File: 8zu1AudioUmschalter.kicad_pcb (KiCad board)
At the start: 2 copper layers, 59 x 65 mm, 63 parts, among them IC1 ATMEGA8A-A, IC2 MAX9890, IC3 TMP75, J1 USB, J2 LUM 1503-07, J3 LUM 1503-07, J4 LUM 1503-07, J5 LUM 1503-07, J6 LUM 1503-07, J7 LUM 1503-07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

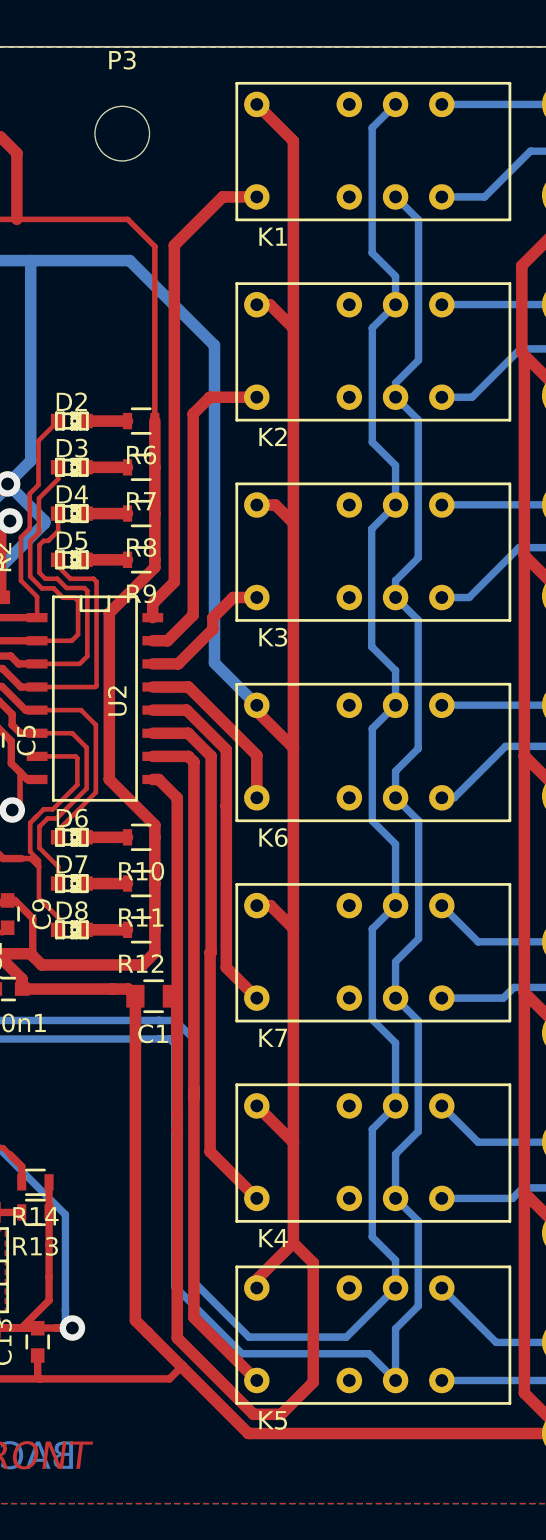
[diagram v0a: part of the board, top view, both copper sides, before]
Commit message: Leitungen zu den Relais auf die Back Layer gelegt
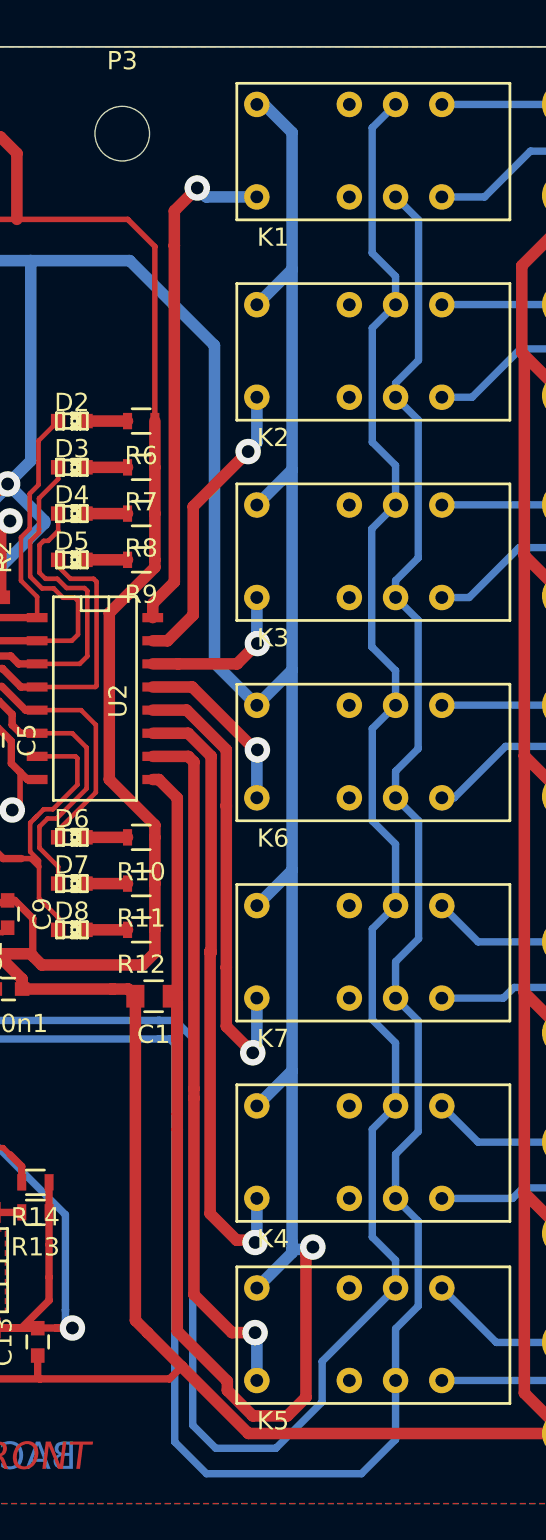
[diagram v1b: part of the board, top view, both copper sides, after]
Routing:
- net /CH_L_REL_IN: track 123.3 -> 134.5 mm
- net /CH_R_REL_IN: track 116.0 -> 127.0 mm
- net Net-(K7-Pad9): track 19.4 -> 25.4 mm, vias 0 -> 1
- net Net-(K4-Pad9): track 29.1 -> 34.7 mm, vias 0 -> 1
- net VCC: track 365.6 -> 367.2 mm, vias 6 -> 7
- net Net-(K1-Pad9): track 26.6 -> 28.1 mm, vias 0 -> 1
- net Net-(K2-Pad9): track 17.7 -> 16.2 mm, vias 0 -> 1
- net Net-(K3-Pad9): track 7.59 -> 8.75 mm, vias 0 -> 1
- net Net-(K5-Pad9): track 38.3 -> 39.0 mm, vias 0 -> 1
- net Net-(K6-Pad9): track 9.60 -> 9.82 mm, vias 0 -> 1

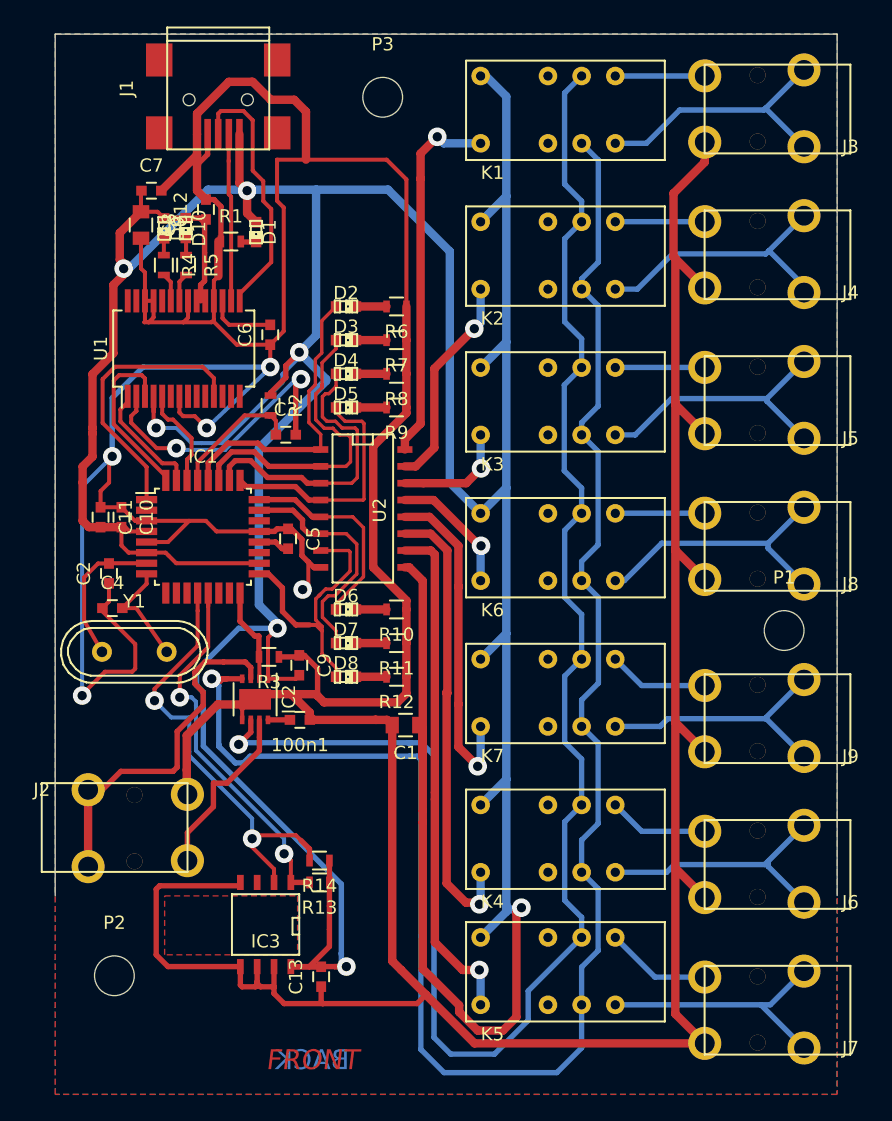
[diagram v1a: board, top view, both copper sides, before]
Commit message: Layoutfehler, TX und RX waren nicht gekreuzt.
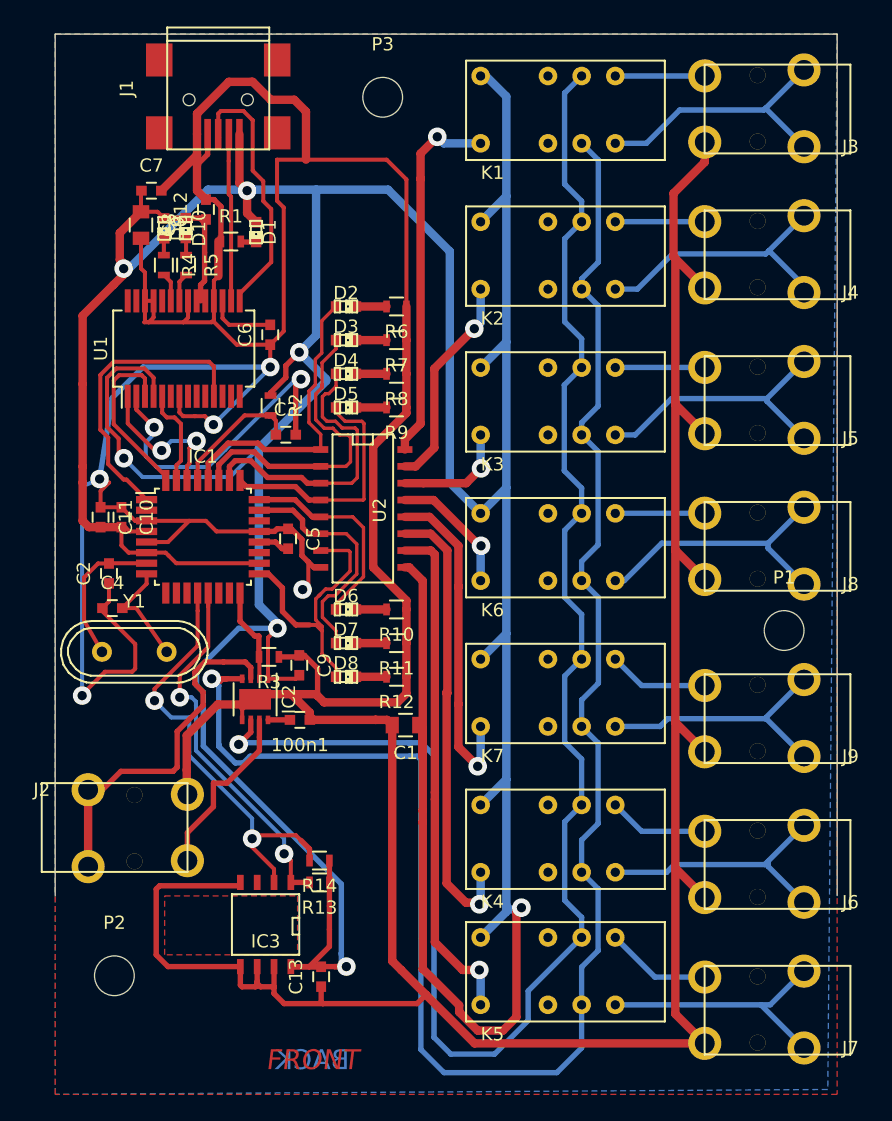
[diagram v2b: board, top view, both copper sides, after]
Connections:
- U1 pad 1: /TX -> /RX
- U1 pad 5: /RX -> /TX
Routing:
- net VCC: track 367.2 -> 372.6 mm
- net /RX: track 7.63 -> 12.2 mm, vias 0 -> 2
- net /DTR: track 22.6 -> 24.7 mm
- net /TX: track 8.88 -> 7.42 mm
- net /CTS: track 21.0 -> 22.4 mm
- net GND: track 425.5 -> 424.6 mm

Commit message: Umpolen der Relais, da diese eine bestimmte Polarität benötigen
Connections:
- K1 pad 8: VCC -> Net-(K1-Pad8)
- K1 pad 9: Net-(K1-Pad9) -> VCC
- K2 pad 8: VCC -> Net-(K2-Pad8)
- K2 pad 9: Net-(K2-Pad9) -> VCC
- K3 pad 8: VCC -> Net-(K3-Pad8)
- K3 pad 9: Net-(K3-Pad9) -> VCC
- K4 pad 8: VCC -> Net-(K4-Pad8)
- K4 pad 9: Net-(K4-Pad9) -> VCC
- K5 pad 8: VCC -> Net-(K5-Pad8)
- K5 pad 9: Net-(K5-Pad9) -> VCC
- K6 pad 8: VCC -> Net-(K6-Pad8)
- K6 pad 9: Net-(K6-Pad9) -> VCC
- K7 pad 8: VCC -> Net-(K7-Pad8)
- K7 pad 9: Net-(K7-Pad9) -> VCC
- U2 pad 10: Net-(K5-Pad9) -> Net-(K5-Pad8)
- U2 pad 11: Net-(K4-Pad9) -> Net-(K4-Pad8)
- U2 pad 12: Net-(K7-Pad9) -> Net-(K7-Pad8)
- U2 pad 13: Net-(K6-Pad9) -> Net-(K6-Pad8)
- U2 pad 14: Net-(K3-Pad9) -> Net-(K3-Pad8)
- U2 pad 15: Net-(K2-Pad9) -> Net-(K2-Pad8)
- U2 pad 16: Net-(K1-Pad9) -> Net-(K1-Pad8)
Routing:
- net Net-(K5-Pad9): track 39.0 -> 0.00 mm, vias 1 -> 0
- net Net-(K4-Pad9): track 34.7 -> 0.00 mm, vias 1 -> 0
- net Net-(K5-Pad8): track 0.00 -> 32.7 mm, vias 0 -> 1
- net Net-(K1-Pad8): track 0.00 -> 30.7 mm, vias 0 -> 1
- net Net-(K1-Pad9): track 28.1 -> 0.00 mm, vias 1 -> 0
- net Net-(K7-Pad9): track 25.4 -> 0.00 mm, vias 1 -> 0
- net Net-(K4-Pad8): track 0.00 -> 24.5 mm, vias 0 -> 1
- net Net-(K2-Pad8): track 0.00 -> 21.5 mm, vias 0 -> 1
- net Net-(K2-Pad9): track 16.2 -> 0.00 mm, vias 1 -> 0
- net Net-(K7-Pad8): track 0.00 -> 14.7 mm, vias 0 -> 1
- net Net-(K3-Pad8): track 0.00 -> 11.7 mm, vias 0 -> 1
- net Net-(K6-Pad9): track 9.82 -> 0.00 mm, vias 1 -> 0
- net VCC: track 372.6 -> 363.6 mm
- net Net-(K3-Pad9): track 8.75 -> 0.00 mm, vias 1 -> 0
- net Net-(K6-Pad8): track 0.00 -> 6.50 mm, vias 0 -> 1
